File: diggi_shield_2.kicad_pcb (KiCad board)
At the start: 4 copper layers, 120 x 100 mm, 101 parts, among them J1_P1 IN_L, J1_P2 IN_GND, J1_P3 IN_R, J1_P4 OUT_R, J1_P5 OUT_GND, J1_P6 OUT_L, J2_P1 HP_R, J2_P2 HP_GND, J2_P3 HP_L, J8_P1 GND, J8_P2 +5V, J8_P3 MIDI_RX*, J8_P4 MIDI_TX, J8_P5 VBUS_END

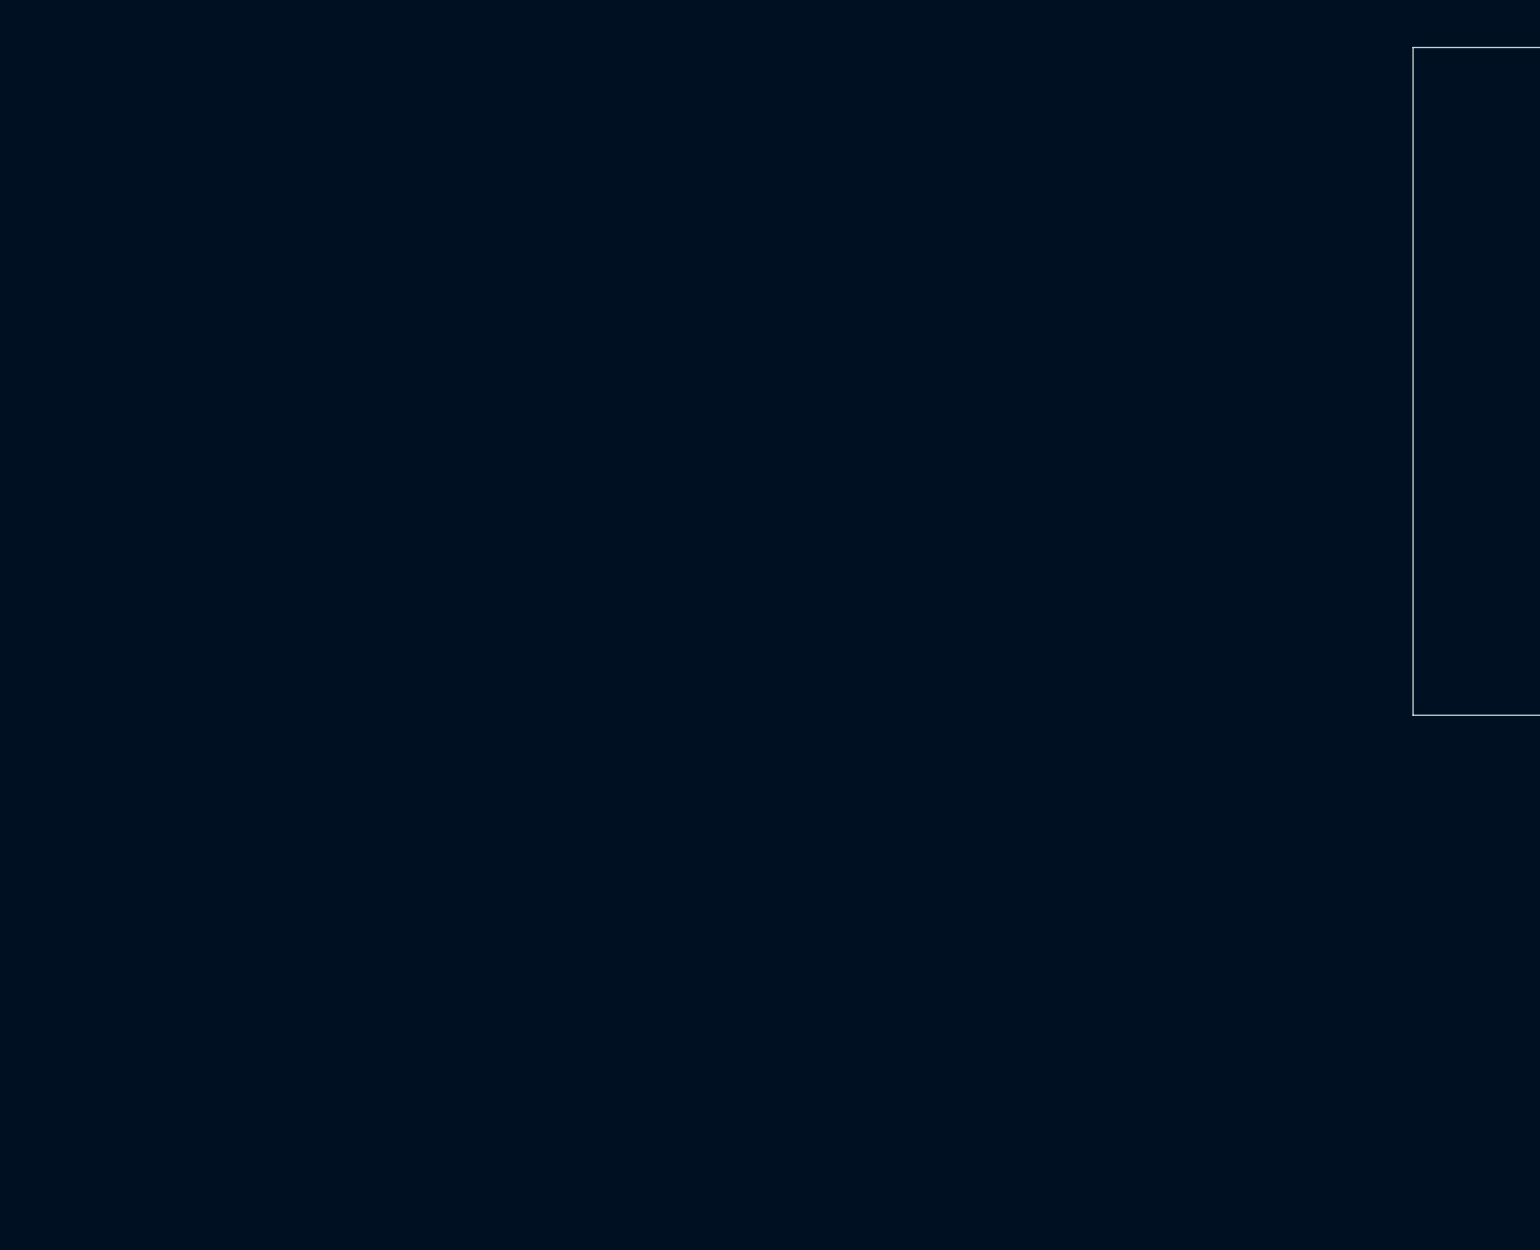
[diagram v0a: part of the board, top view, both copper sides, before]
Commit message: Added jack symbols and footprints also footprints for ics and caps
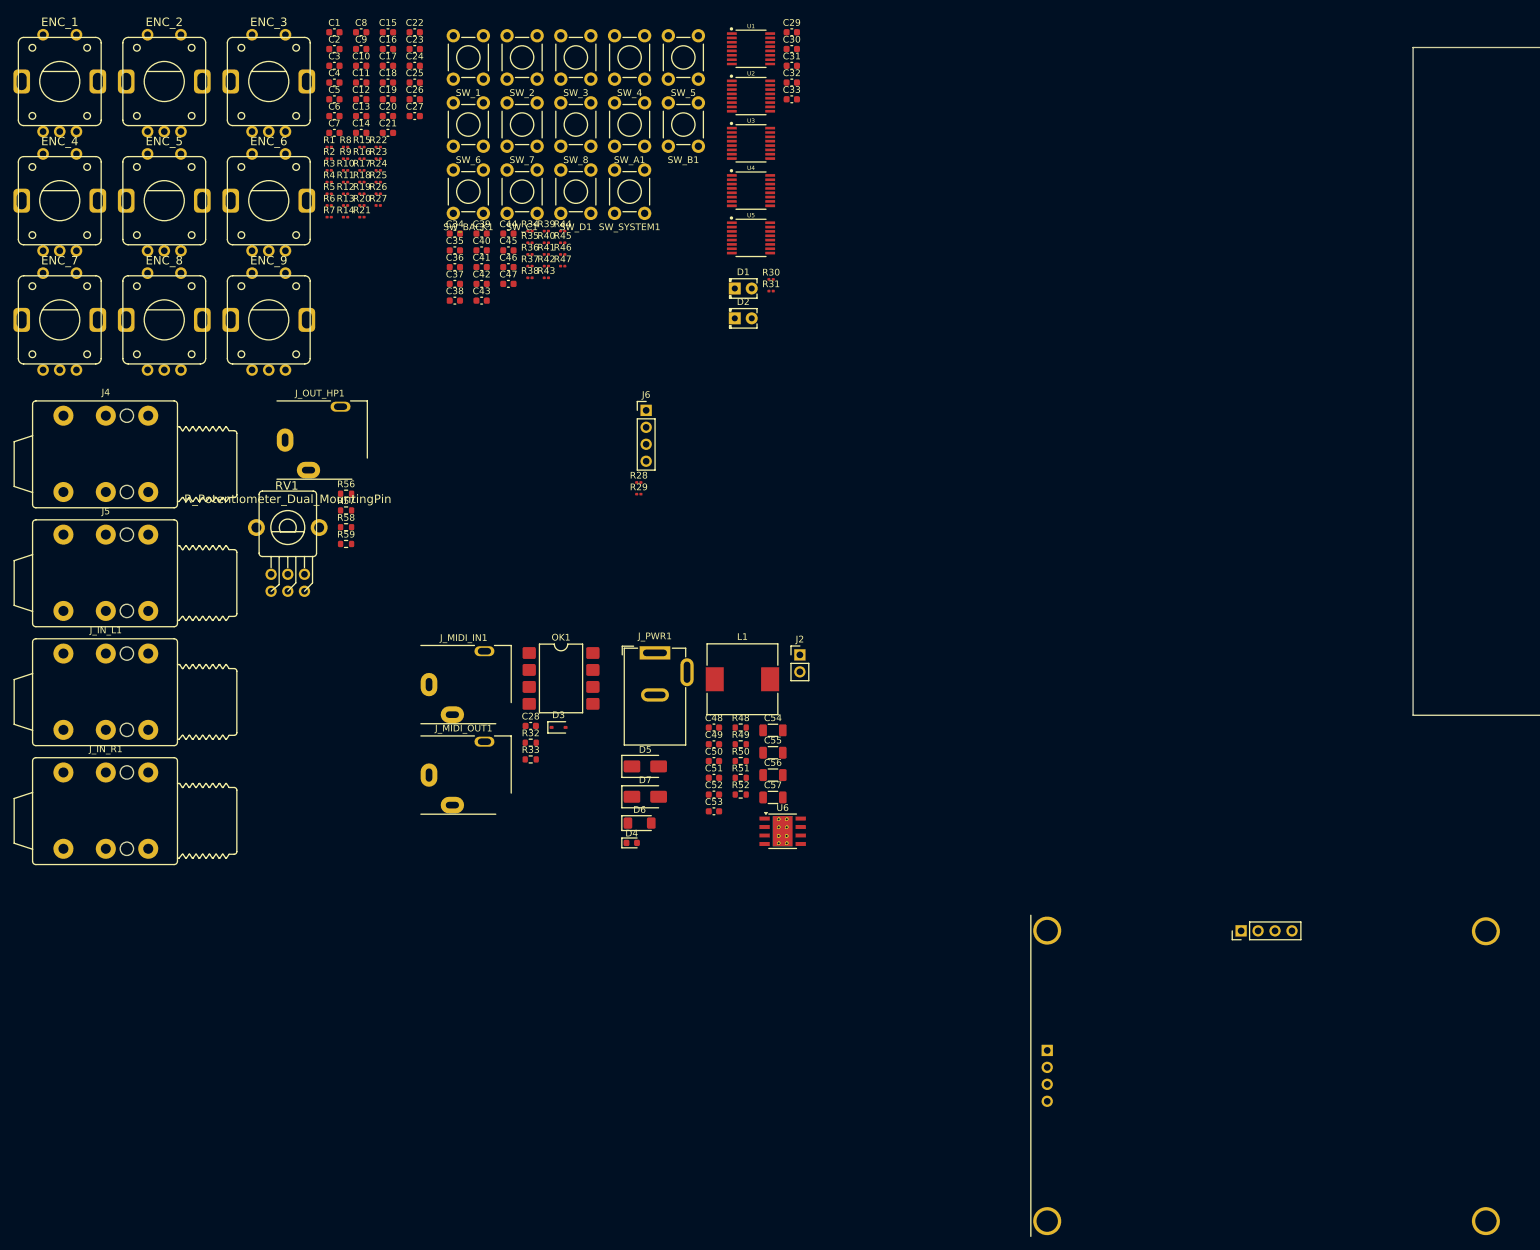
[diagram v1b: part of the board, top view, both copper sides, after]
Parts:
- added C1: 100nf, Capacitor_SMD:C_0603_1608Metric, F.Cu at (-72.9, 43.2)
- added C10: 100nf, Capacitor_SMD:C_0603_1608Metric, F.Cu at (-68.9, 48.2)
- added C11: 100nf, Capacitor_SMD:C_0603_1608Metric, F.Cu at (-68.9, 50.7)
- added C12: 100nf, Capacitor_SMD:C_0603_1608Metric, F.Cu at (-68.9, 53.2)
- added C13: 100nf, Capacitor_SMD:C_0603_1608Metric, F.Cu at (-68.9, 55.7)
- added C14: 100nf, Capacitor_SMD:C_0603_1608Metric, F.Cu at (-68.9, 58.2)
- added C15: 100nf, Capacitor_SMD:C_0603_1608Metric, F.Cu at (-64.9, 43.2)
- added C16: 100nf, Capacitor_SMD:C_0603_1608Metric, F.Cu at (-64.9, 45.7)
- added C17: 100nf, Capacitor_SMD:C_0603_1608Metric, F.Cu at (-64.9, 48.2)
- added C18: 100nf, Capacitor_SMD:C_0603_1608Metric, F.Cu at (-64.9, 50.7)
- added C19: 100nf, Capacitor_SMD:C_0603_1608Metric, F.Cu at (-64.9, 53.2)
- added C2: 100nf, Capacitor_SMD:C_0603_1608Metric, F.Cu at (-72.9, 45.7)
- added C20: 100nf, Capacitor_SMD:C_0603_1608Metric, F.Cu at (-64.9, 55.7)
- added C21: 100nf, Capacitor_SMD:C_0603_1608Metric, F.Cu at (-64.9, 58.2)
- added C22: 100nf, Capacitor_SMD:C_0603_1608Metric, F.Cu at (-60.9, 43.2)
- added C23: 100nf, Capacitor_SMD:C_0603_1608Metric, F.Cu at (-60.9, 45.7)
- added C24: 100nf, Capacitor_SMD:C_0603_1608Metric, F.Cu at (-60.9, 48.2)
- added C25: 100nf, Capacitor_SMD:C_0603_1608Metric, F.Cu at (-60.9, 50.7)
- added C26: 100nf, Capacitor_SMD:C_0603_1608Metric, F.Cu at (-60.9, 53.2)
- added C27: 100nf, Capacitor_SMD:C_0603_1608Metric, F.Cu at (-60.9, 55.7)
- added C28: 100nf, Capacitor_SMD:C_0603_1608Metric, F.Cu at (-43.5, 147.1)
- added C29: 100nf, Capacitor_SMD:C_0603_1608Metric, F.Cu at (-4.45, 43.2)
- added C3: 100nf, Capacitor_SMD:C_0603_1608Metric, F.Cu at (-72.9, 48.2)
- added C30: 100nf, Capacitor_SMD:C_0603_1608Metric, F.Cu at (-4.45, 45.7)
- added C31: 100nf, Capacitor_SMD:C_0603_1608Metric, F.Cu at (-4.45, 48.2)
- added C32: 100nf, Capacitor_SMD:C_0603_1608Metric, F.Cu at (-4.45, 50.7)
- added C33: 100nf, Capacitor_SMD:C_0603_1608Metric, F.Cu at (-4.45, 53.2)
- added C34: 100nf, Capacitor_SMD:C_0603_1608Metric, F.Cu at (-54.9, 73.3)
- added C35: 100nf, Capacitor_SMD:C_0603_1608Metric, F.Cu at (-54.9, 75.8)
- added C36: 100nf, Capacitor_SMD:C_0603_1608Metric, F.Cu at (-54.9, 78.4)
- added C37: 100nf, Capacitor_SMD:C_0603_1608Metric, F.Cu at (-54.9, 80.9)
- added C38: 100nf, Capacitor_SMD:C_0603_1608Metric, F.Cu at (-54.9, 83.4)
- added C39: 100nf, Capacitor_SMD:C_0603_1608Metric, F.Cu at (-50.9, 73.3)
- added C4: 100nf, Capacitor_SMD:C_0603_1608Metric, F.Cu at (-72.9, 50.7)
- added C40: 100nf, Capacitor_SMD:C_0603_1608Metric, F.Cu at (-50.9, 75.8)
- added C41: 100nf, Capacitor_SMD:C_0603_1608Metric, F.Cu at (-50.9, 78.4)
- added C42: 100nf, Capacitor_SMD:C_0603_1608Metric, F.Cu at (-50.9, 80.9)
- added C43: 100nf, Capacitor_SMD:C_0603_1608Metric, F.Cu at (-50.9, 83.4)
- added C44: 100nf, Capacitor_SMD:C_0603_1608Metric, F.Cu at (-46.9, 73.3)
- added C45: 100nf, Capacitor_SMD:C_0603_1608Metric, F.Cu at (-46.9, 75.8)
- added C46: 100nf, Capacitor_SMD:C_0603_1608Metric, F.Cu at (-46.9, 78.4)
- added C47: 100nf, Capacitor_SMD:C_0603_1608Metric, F.Cu at (-46.9, 80.9)
- added C48: 100n, Capacitor_SMD:C_0603_1608Metric, F.Cu at (-16.1, 147.3)
- added C49: 10u, Capacitor_SMD:C_0603_1608Metric, F.Cu at (-16.1, 149.8)
- added C5: 100nf, Capacitor_SMD:C_0603_1608Metric, F.Cu at (-72.9, 53.2)
- added C50: 10u, Capacitor_SMD:C_0603_1608Metric, F.Cu at (-16.1, 152.3)
- added C51: 100n, Capacitor_SMD:C_0603_1608Metric, F.Cu at (-16.1, 154.8)
- added C52: 10n, Capacitor_SMD:C_0603_1608Metric, F.Cu at (-16.1, 157.3)
- added C53: 100n, Capacitor_SMD:C_0603_1608Metric, F.Cu at (-16.1, 159.9)
- added C54: 47u, Capacitor_SMD:C_1206_3216Metric, F.Cu at (-7.27, 147.7)
- added C55: 47u, Capacitor_SMD:C_1206_3216Metric, F.Cu at (-7.27, 151.1)
- added C56: 47u, Capacitor_SMD:C_1206_3216Metric, F.Cu at (-7.27, 154.4)
- added C57: 47u, Capacitor_SMD:C_1206_3216Metric, F.Cu at (-7.27, 157.8)
- added C6: 100nf, Capacitor_SMD:C_0603_1608Metric, F.Cu at (-72.9, 55.7)
- added C7: 100nf, Capacitor_SMD:C_0603_1608Metric, F.Cu at (-72.9, 58.2)
- added C8: 100nf, Capacitor_SMD:C_0603_1608Metric, F.Cu at (-68.9, 43.2)
- added C9: 100nf, Capacitor_SMD:C_0603_1608Metric, F.Cu at (-68.9, 45.7)
- added D1: LED, LED_THT:LED_D2.0mm_W4.0mm_H2.8mm_FlatTop, F.Cu at (-13.0, 81.6)
- added D2: LED, LED_THT:LED_D2.0mm_W4.0mm_H2.8mm_FlatTop, F.Cu at (-13.0, 86.0)
- added D3: 1N4148WS, Diode_SMD:D_SOD-323, F.Cu at (-39.4, 147.3)
- added D4: LED, LED_SMD:LED_0603_1608Metric, F.Cu at (-28.4, 164.6)
- added D5: SS34, Diode_SMD:D_SMA, F.Cu at (-26.4, 153.1)
- added D6: 3V3, Diode_SMD:D_MiniMELF, F.Cu at (-27.2, 161.6)
- added D7: SS34, Diode_SMD:D_SMA, F.Cu at (-26.4, 157.7)
- added ENC_1: Encoder1, ksoloti_shield_footprints:ALPS_STEC12E08, F.Cu at (-114.1, 50.6)
- added ENC_2: Encoder2, ksoloti_shield_footprints:ALPS_STEC12E08, F.Cu at (-98.4, 50.6)
- added ENC_3: Encoder3, ksoloti_shield_footprints:ALPS_STEC12E08, F.Cu at (-82.8, 50.6)
- added ENC_4: Encoder4, ksoloti_shield_footprints:ALPS_STEC12E08, F.Cu at (-114.1, 68.4)
- added ENC_5: Encoder5, ksoloti_shield_footprints:ALPS_STEC12E08, F.Cu at (-98.4, 68.4)
- added ENC_6: Encoder6, ksoloti_shield_footprints:ALPS_STEC12E08, F.Cu at (-82.8, 68.4)
- added ENC_7: Encoder7, ksoloti_shield_footprints:ALPS_STEC12E08, F.Cu at (-114.1, 86.3)
- added ENC_8: Encoder8, ksoloti_shield_footprints:ALPS_STEC12E08, F.Cu at (-98.4, 86.3)
- added ENC_9: Encoder9, ksoloti_shield_footprints:ALPS_STEC12E08, F.Cu at (-82.8, 86.3)
- added J2: VIN, Connector_PinHeader_2.54mm:PinHeader_1x02_P2.54mm_Vertical, F.Cu at (-3.24, 136.4)
- added J4: Out Left, ksoloti_shield_footprints:Jack_6.35mm_Neutrik_NRJ6HF_Horizontal_no_screwhole, F.Cu at (-113.5, 100.6)
- added J5: Out Right, ksoloti_shield_footprints:Jack_6.35mm_Neutrik_NRJ6HF_Horizontal_no_screwhole, F.Cu at (-113.5, 118.4)
- added J6: I2C_HEADER, Connector_PinHeader_2.54mm:PinHeader_1x04_P2.54mm_Vertical, F.Cu at (-26.3, 99.8)
- added J_IN_L1: In Left, ksoloti_shield_footprints:Jack_6.35mm_Neutrik_NRJ6HF_Horizontal_no_screwhole, F.Cu at (-113.5, 136.2)
- added J_IN_R1: In Right, ksoloti_shield_footprints:Jack_6.35mm_Neutrik_NRJ6HF_Horizontal_no_screwhole, F.Cu at (-113.5, 154.0)
- added J_MIDI_IN1: Midi In Jack, Connector_Audio:Jack_3.5mm_CUI_SJ1-3513N_Horizontal, F.Cu at (-58.8, 140.9)
- added J_MIDI_OUT1: Midi Out Jack, Connector_Audio:Jack_3.5mm_CUI_SJ1-3513N_Horizontal, F.Cu at (-58.8, 154.4)
- added J_OUT_HP1: Headphones Out, Connector_Audio:Jack_3.5mm_CUI_SJ1-3513N_Horizontal, F.Cu at (-80.3, 104.3)
- added J_PWR1: DC 9-20V, Connector_BarrelJack:BarrelJack_GCT_DCJ200-10-A_Horizontal, F.Cu at (-24.9, 136.1)
- added L1: 15uh, Inductor_SMD:L_10.4x10.4_H4.8, F.Cu at (-11.8, 140.1)
- added OK1: 6N137, Package_DIP:SMDIP-8_W9.53mm, F.Cu at (-39.0, 140.0)
- added OLED1: 128x64_OLED, diggi_footprints:2.42 OLED Simon Karl Custom, F.Cu at (66.7, 177.8)
- added R1: 10k, Resistor_SMD:R_0201_0603Metric, F.Cu at (-73.7, 60.4)
- added R10: 10k, Resistor_SMD:R_0201_0603Metric, F.Cu at (-71.3, 63.9)
- added R11: 10k, Resistor_SMD:R_0201_0603Metric, F.Cu at (-71.3, 65.6)
- added R12: 10k, Resistor_SMD:R_0201_0603Metric, F.Cu at (-71.3, 67.4)
- added R13: 10k, Resistor_SMD:R_0201_0603Metric, F.Cu at (-71.3, 69.1)
- added R14: 10k, Resistor_SMD:R_0201_0603Metric, F.Cu at (-71.3, 70.9)
- added R15: 10k, Resistor_SMD:R_0201_0603Metric, F.Cu at (-68.8, 60.4)
- added R16: 10k, Resistor_SMD:R_0201_0603Metric, F.Cu at (-68.8, 62.1)
- added R17: 10k, Resistor_SMD:R_0201_0603Metric, F.Cu at (-68.8, 63.9)
- added R18: 10k, Resistor_SMD:R_0201_0603Metric, F.Cu at (-68.8, 65.6)
- added R19: 10k, Resistor_SMD:R_0201_0603Metric, F.Cu at (-68.8, 67.4)
- added R2: 10k, Resistor_SMD:R_0201_0603Metric, F.Cu at (-73.7, 62.1)
- added R20: 10k, Resistor_SMD:R_0201_0603Metric, F.Cu at (-68.8, 69.1)
- added R21: 10k, Resistor_SMD:R_0201_0603Metric, F.Cu at (-68.8, 70.9)
- added R22: 10k, Resistor_SMD:R_0201_0603Metric, F.Cu at (-66.4, 60.4)
- added R23: 10k, Resistor_SMD:R_0201_0603Metric, F.Cu at (-66.4, 62.1)
- added R24: 10k, Resistor_SMD:R_0201_0603Metric, F.Cu at (-66.4, 63.9)
- added R25: 10k, Resistor_SMD:R_0201_0603Metric, F.Cu at (-66.4, 65.6)
- added R26: 10k, Resistor_SMD:R_0201_0603Metric, F.Cu at (-66.4, 67.4)
- added R27: 10k, Resistor_SMD:R_0201_0603Metric, F.Cu at (-66.4, 69.1)
- added R28: 2.7k, Resistor_SMD:R_0201_0603Metric, F.Cu at (-27.4, 110.6)
- added R29: 2.7k, Resistor_SMD:R_0201_0603Metric, F.Cu at (-27.4, 112.4)
- added R3: 10k, Resistor_SMD:R_0201_0603Metric, F.Cu at (-73.7, 63.9)
- added R30: 220, Resistor_SMD:R_0201_0603Metric, F.Cu at (-7.55, 80.2)
- added R31: 320, Resistor_SMD:R_0201_0603Metric, F.Cu at (-7.55, 81.9)
- added R32: 220, Resistor_SMD:R_0603_1608Metric, F.Cu at (-43.5, 149.6)
- added R33: 10k, Resistor_SMD:R_0603_1608Metric, F.Cu at (-43.5, 152.1)
- added R34: 10k, Resistor_SMD:R_0201_0603Metric, F.Cu at (-43.7, 73.0)
- added R35: 10k, Resistor_SMD:R_0201_0603Metric, F.Cu at (-43.7, 74.7)
- added R36: 10k, Resistor_SMD:R_0201_0603Metric, F.Cu at (-43.7, 76.5)
- added R37: 10k, Resistor_SMD:R_0201_0603Metric, F.Cu at (-43.7, 78.2)
- added R38: 10k, Resistor_SMD:R_0201_0603Metric, F.Cu at (-43.7, 80.0)
- added R39: 10k, Resistor_SMD:R_0201_0603Metric, F.Cu at (-41.2, 73.0)
- added R4: 10k, Resistor_SMD:R_0201_0603Metric, F.Cu at (-73.7, 65.6)
- added R40: 10k, Resistor_SMD:R_0201_0603Metric, F.Cu at (-41.2, 74.7)
- added R41: 10k, Resistor_SMD:R_0201_0603Metric, F.Cu at (-41.2, 76.5)
- added R42: 10k, Resistor_SMD:R_0201_0603Metric, F.Cu at (-41.2, 78.2)
- added R43: 10k, Resistor_SMD:R_0201_0603Metric, F.Cu at (-41.2, 80.0)
- added R44: 10k, Resistor_SMD:R_0201_0603Metric, F.Cu at (-38.8, 73.0)
- added R45: 10k, Resistor_SMD:R_0201_0603Metric, F.Cu at (-38.8, 74.7)
- added R46: 10k, Resistor_SMD:R_0201_0603Metric, F.Cu at (-38.8, 76.5)
- added R47: 10k, Resistor_SMD:R_0201_0603Metric, F.Cu at (-38.8, 78.2)
- added R48: 47k, Resistor_SMD:R_0603_1608Metric, F.Cu at (-12.1, 147.3)
- added R49: 10k, Resistor_SMD:R_0603_1608Metric, F.Cu at (-12.1, 149.8)
- added R5: 10k, Resistor_SMD:R_0201_0603Metric, F.Cu at (-73.7, 67.4)
- added R50: 10k, Resistor_SMD:R_0603_1608Metric, F.Cu at (-12.1, 152.3)
- added R51: 220, Resistor_SMD:R_0603_1608Metric, F.Cu at (-12.1, 154.8)
- added R52: 3k, Resistor_SMD:R_0603_1608Metric, F.Cu at (-12.1, 157.3)
- added R56: 220, Resistor_SMD:R_0603_1608Metric, F.Cu at (-71.2, 112.3)
- added R57: 47k, Resistor_SMD:R_0603_1608Metric, F.Cu at (-71.2, 114.8)
- added R58: 47k, Resistor_SMD:R_0603_1608Metric, F.Cu at (-71.2, 117.3)
- added R59: 220, Resistor_SMD:R_0603_1608Metric, F.Cu at (-71.2, 119.8)
- added R6: 10k, Resistor_SMD:R_0201_0603Metric, F.Cu at (-73.7, 69.1)
- added R7: 10k, Resistor_SMD:R_0201_0603Metric, F.Cu at (-73.7, 70.9)
- added R8: 10k, Resistor_SMD:R_0201_0603Metric, F.Cu at (-71.3, 60.4)
- added R9: 10k, Resistor_SMD:R_0201_0603Metric, F.Cu at (-71.3, 62.1)
- added RV1: R_Potentiometer_Dual_MountingPin, ksoloti_shield_footprints:ALPS_POT_VERTICAL_PS_DUAL, F.Cu at (-79.9, 117.4)
- added SW_1: sw_1, ksoloti_shield_footprints:TL1105T, F.Cu at (-52.9, 47.0)
- added SW_2: sw_2, ksoloti_shield_footprints:TL1105T, F.Cu at (-44.8, 47.0)
- added SW_3: sw_3, ksoloti_shield_footprints:TL1105T, F.Cu at (-36.8, 47.0)
- added SW_4: sw_4, ksoloti_shield_footprints:TL1105T, F.Cu at (-28.7, 47.0)
- added SW_5: sw_5, ksoloti_shield_footprints:TL1105T, F.Cu at (-20.7, 47.0)
- added SW_6: sw_6, ksoloti_shield_footprints:TL1105T, F.Cu at (-52.9, 57.0)
- added SW_7: sw_7, ksoloti_shield_footprints:TL1105T, F.Cu at (-44.8, 57.0)
- added SW_8: sw_8, ksoloti_shield_footprints:TL1105T, F.Cu at (-36.8, 57.0)
- added SW_A1: sw_a, ksoloti_shield_footprints:TL1105T, F.Cu at (-28.7, 57.0)
- added SW_B1: sw_b, ksoloti_shield_footprints:TL1105T, F.Cu at (-20.7, 57.0)
- added SW_BACK1: back, ksoloti_shield_footprints:TL1105T, F.Cu at (-52.9, 67.1)
- added SW_C1: sw_c, ksoloti_shield_footprints:TL1105T, F.Cu at (-44.8, 67.1)
- added SW_D1: sw_d, ksoloti_shield_footprints:TL1105T, F.Cu at (-36.8, 67.1)
- added SW_SYSTEM1: system, ksoloti_shield_footprints:TL1105T, F.Cu at (-28.7, 67.1)
- added U1: 74HC165, diggi_footprints:SOP65P640X120-16, F.Cu at (-10.6, 45.7)
- added U2: 74HC165, diggi_footprints:SOP65P640X120-16, F.Cu at (-10.6, 52.7)
- added U3: 74HC165, diggi_footprints:SOP65P640X120-16, F.Cu at (-10.6, 59.8)
- added U4: 74HC165, diggi_footprints:SOP65P640X120-16, F.Cu at (-10.6, 66.9)
- added U5: 74HC165, diggi_footprints:SOP65P640X120-16, F.Cu at (-10.6, 74.0)
- added U6: TPS5430DDA, Package_SO:TI_SO-PowerPAD-8_ThermalVias, F.Cu at (-5.82, 162.8)
